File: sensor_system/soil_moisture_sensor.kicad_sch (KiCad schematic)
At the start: 15 parts, among them U1 TLC555xD, U2 XC6206PxxxMR

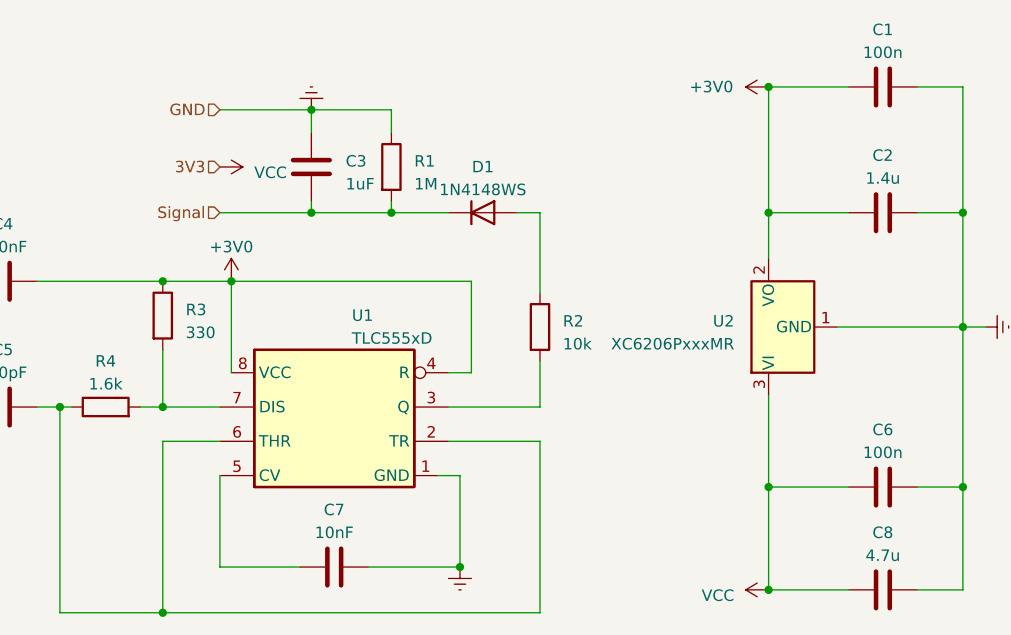
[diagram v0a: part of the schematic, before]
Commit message: Pievienoti footprint visām komponentēm
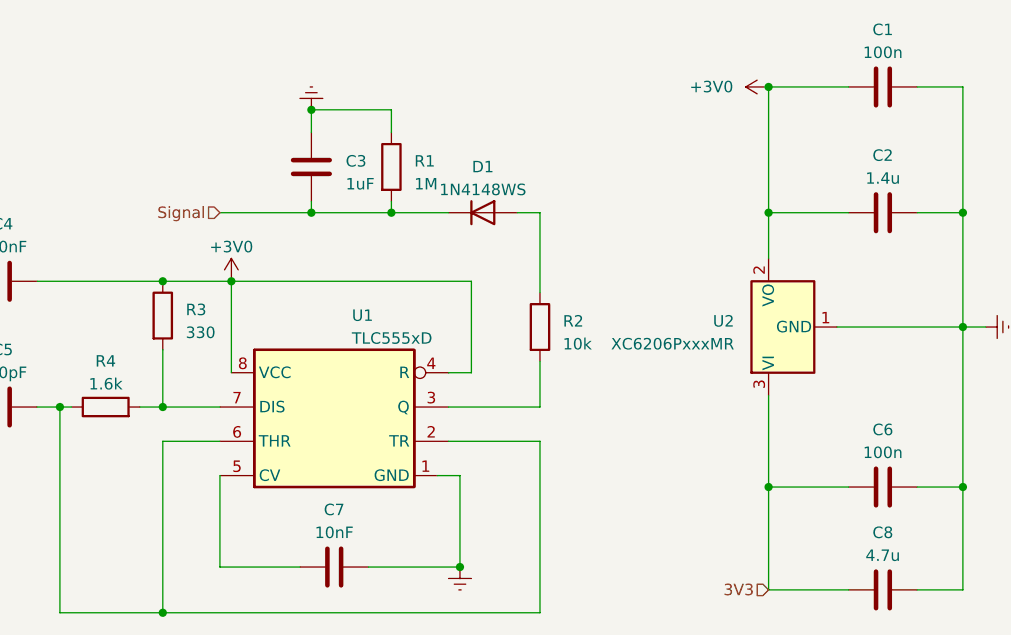
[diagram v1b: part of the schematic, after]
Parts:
- C1, C4, C5, C6, C7, R1, R2, R3, R4: footprint (none) -> Resistor_SMD:R_0805_2012Metric
- C2, C8: footprint (none) -> Capacitor_SMD:C_0805_2012Metric
- C3: footprint (none) -> Capacitor_SMD:C_0603_1608Metric
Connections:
- net VCC renamed 3V3
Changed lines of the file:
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@@
   (junction (at 149.86 95.25) (diameter 0) (color 0 0 0 0)
   )
-  (junction (at 200.66 137.16) (diameter 0) (color 0 0 0 0)
-  )
   (junction (at 158.75 95.25) (diameter 0) (color 0 0 0 0)
   )
@@
     (stroke (width 0) (type default))
   )
+  (wire (pts (xy 200.66 137.16) (xy 209.55 137.16))
+    (stroke (width 0) (type default))
+  )
   (wire (pts (xy 200.66 95.25) (xy 209.55 95.25))
     (stroke (width 0) (type default))
@@
     (stroke (width 0) (type default))
   )
-  (wire (pts (xy 200.66 137.16) (xy 200.66 125.73))
-    (stroke (width 0) (type default))
-  )
   (wire (pts (xy 222.25 125.73) (xy 222.25 107.95))
     (stroke (width 0) (type default))
@@
     (stroke (width 0) (type default))
   )
-  (wire (pts (xy 209.55 137.16) (xy 200.66 137.16))
-    (stroke (width 0) (type default))
-  )
   (wire (pts (xy 121.92 116.84) (xy 123.19 116.84))
     (stroke (width 0) (type default))
@@
     (stroke (width 0) (type default))
   )
-  (wire (pts (xy 139.7 83.82) (xy 149.86 83.82))
-    (stroke (width 0) (type default))
-  )
   (wire (pts (xy 222.25 125.73) (xy 222.25 137.16))
     (stroke (width 0) (type default))
@@
     (stroke (width 0) (type default))
   )
+  (wire (pts (xy 200.66 125.73) (xy 200.66 137.16))
+    (stroke (width 0) (type default))
+  )
   (wire (pts (xy 217.17 125.73) (xy 222.25 125.73))
     (stroke (width 0) (type default))
@@
     (stroke (width 0) (type default))
   )
-  (hierarchical_label "3V3" (shape input) (at 139.7 90.17 180) (fields_autoplaced)
+  (hierarchical_label "3V3" (shape input) (at 200.66 137.16 180) (fields_autoplaced)
     (effects (font (size 1.27 1.27)) (justify right))
   )
   (hierarchical_label "Signal" (shape input) (at 139.7 95.25 180) (fields_autoplaced)
-    (effects (font (size 1.27 1.27)) (justify right))
-  )
-  (hierarchical_label "GND" (shape input) (at 139.7 83.82 180) (fields_autoplaced)
     (effects (font (size 1.27 1.27)) (justify right))
   )
@@
       (effects (font (size 1.27 1.27)))
     )
-    (property "Footprint" "" (at 217.17 124.7648 0)
+    (property "Footprint" "Resistor_SMD:R_0805_2012Metric" (at 217.17 124.7648 0)
       (effects (font (size 1.27 1.27)) hide)
     )
@@
       (effects (font (size 1.27 1.27)))
     )
-    (property "Footprint" "" (at 119.38 101.9048 0)
+    (property "Footprint" "Resistor_SMD:R_0805_2012Metric" (at 119.38 101.9048 0)
       (effects (font (size 1.27 1.27)) hide)
     )
@@
       (effects (font (size 1.27 1.27)))
     )
-    (property "Footprint" "" (at 119.38 115.8748 0)
+    (property "Footprint" "Resistor_SMD:R_0805_2012Metric" (at 119.38 115.8748 0)
       (effects (font (size 1.27 1.27)) hide)
     )
@@
       (effects (font (size 1.27 1.27)))
     )
-    (property "Footprint" "" (at 127 118.618 90)
+    (property "Footprint" "Resistor_SMD:R_0805_2012Metric" (at 127 118.618 90)
       (effects (font (size 1.27 1.27)) hide)
     )
@@
       (effects (font (size 1.27 1.27)))
     )
-    (property "Footprint" "" (at 156.21 133.6548 0)
+    (property "Footprint" "Resistor_SMD:R_0805_2012Metric" (at 156.21 133.6548 0)
       (effects (font (size 1.27 1.27)) hide)
     )
@@
       (effects (font (size 1.27 1.27)))
     )
-    (property "Footprint" "" (at 217.17 94.2848 0)
+    (property "Footprint" "Capacitor_SMD:C_0805_2012Metric" (at 217.17 94.2848 0)
       (effects (font (size 1.27 1.27)) hide)
     )
@@
       (effects (font (size 1.27 1.27)) (justify left))
     )
-    (property "Footprint" "" (at 150.8252 93.98 0)
+    (property "Footprint" "Capacitor_SMD:C_0603_1608Metric" (at 150.8252 93.98 0)
       (effects (font (size 1.27 1.27)) hide)
     )
@@
       (effects (font (size 1.27 1.27)) (justify left))
     )
-    (property "Footprint" "" (at 131.572 106.68 90)
+    (property "Footprint" "Resistor_SMD:R_0805_2012Metric" (at 131.572 106.68 90)
       (effects (font (size 1.27 1.27)) hide)
     )
@@
       (effects (font (size 1.27 1.27)) (justify left))
     )
-    (property "Footprint" "" (at 156.972 90.17 90)
+    (property "Footprint" "Resistor_SMD:R_0805_2012Metric" (at 156.972 90.17 90)
       (effects (font (size 1.27 1.27)) hide)
     )
@@
       (effects (font (size 1.27 1.27)) (justify left))
     )
-    (property "Footprint" "" (at 173.482 107.95 90)
+    (property "Footprint" "Resistor_SMD:R_0805_2012Metric" (at 173.482 107.95 90)
       (effects (font (size 1.27 1.27)) hide)
     )
@@
       (effects (font (size 1.27 1.27)))
     )
-    (property "Footprint" "" (at 217.17 136.1948 0)
+    (property "Footprint" "Capacitor_SMD:C_0805_2012Metric" (at 217.17 136.1948 0)
       (effects (font (size 1.27 1.27)) hide)
     )
@@
       (effects (font (size 1.27 1.27)))
     )
-    (property "Footprint" "" (at 217.17 80.3148 0)
+    (property "Footprint" "Resistor_SMD:R_0805_2012Metric" (at 217.17 80.3148 0)
       (effects (font (size 1.27 1.27)) hide)
     )
@@
         )
       )
-    )
-  )
-  (symbol (lib_id "power:VCC") (at 200.66 137.16 90) (unit 1)
-    (in_bom yes) (on_board yes) (dnp no) (fields_autoplaced)
-    (property "Reference" "#PWR08" (at 204.47 137.16 0)
-      (effects (font (size 1.27 1.27)) hide)
-    )
-    (property "Value" "VCC" (at 196.85 137.795 90)
-      (effects (font (size 1.27 1.27)) (justify left))
-    )
-    (property "Footprint" "" (at 200.66 137.16 0)
-      (effects (font (size 1.27 1.27)) hide)
-    )
-    (property "Datasheet" "" (at 200.66 137.16 0)
-      (effects (font (size 1.27 1.27)) hide)
-    )
-    (pin "1")
-    (instances
-      (project "sensor_system"
-        (path "/d745cb62-8f4d-408c-9af8-25e31ee1e0d0/aa2079c6-27cc-4f87-ae93-44912efb1889"
-          (reference "#PWR08") (unit 1)
-        )
-      )
-    )
-  )
-  (symbol (lib_id "power:VCC") (at 139.7 90.17 270) (unit 1)
-    (in_bom yes) (on_board yes) (dnp no) (fields_autoplaced)
-    (property "Reference" "#PWR04" (at 135.89 90.17 0)
-      (effects (font (size 1.27 1.27)) hide)
-    )
-    (property "Value" "VCC" (at 143.51 90.805 90)
-      (effects (font (size 1.27 1.27)) (justify left))
-    )
-    (property "Footprint" "" (at 139.7 90.17 0)
-      (effects (font (size 1.27 1.27)) hide)
-    )
-    (property "Datasheet" "" (at 139.7 90.17 0)
-      (effects (font (size 1.27 1.27)) hide)
-    )
-    (pin "1")
-    (instances
-      (project "sensor_system"
-        (path "/d745cb62-8f4d-408c-9af8-25e31ee1e0d0/aa2079c6-27cc-4f87-ae93-44912efb1889"
-          (reference "#PWR04") (unit 1)
-        )
-      )

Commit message: Disaster in progress
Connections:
- net +3V0 renamed 3V
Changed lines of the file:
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@@
 (kicad_sch (version 20230121) (generator eeschema)
   (paper "A4")
-  (junction (at 200.66 81.28) (diameter 0) (color 0 0 0 0)
-  )
   (junction (at 140.97 102.87) (diameter 0) (color 0 0 0 0)
   )
@@
     (stroke (width 0) (type default))
   )
-  (wire (pts (xy 167.64 102.87) (xy 140.97 102.87))
-    (stroke (width 0) (type default))
-  )
   (wire (pts (xy 149.86 95.25) (xy 158.75 95.25))
     (stroke (width 0) (type default))
@@
     (stroke (width 0) (type default))
   )
+  (wire (pts (xy 140.97 102.87) (xy 167.64 102.87))
+    (stroke (width 0) (type default))
+  )
   (wire (pts (xy 200.66 137.16) (xy 209.55 137.16))
     (stroke (width 0) (type default))
@@
     (stroke (width 0) (type default))
   )
+  (wire (pts (xy 158.75 83.82) (xy 158.75 86.36))
+    (stroke (width 0) (type default))
+  )
+  (wire (pts (xy 140.97 102.87) (xy 133.35 102.87))
+    (stroke (width 0) (type default))
+  )
+  (wire (pts (xy 140.97 102.87) (xy 140.97 113.03))
+    (stroke (width 0) (type default))
+  )
+  (wire (pts (xy 175.26 95.25) (xy 172.72 95.25))
+    (stroke (width 0) (type default))
+  )
+  (wire (pts (xy 156.21 134.62) (xy 166.37 134.62))
+    (stroke (width 0) (type default))
+  )
+  (wire (pts (xy 222.25 125.73) (xy 222.25 137.16))
+    (stroke (width 0) (type default))
+  )
+  (wire (pts (xy 133.35 120.65) (xy 133.35 139.7))
+    (stroke (width 0) (type default))
+  )
+  (wire (pts (xy 208.28 107.95) (xy 222.25 107.95))
+    (stroke (width 0) (type default))
+  )
+  (wire (pts (xy 167.64 113.03) (xy 167.64 102.87))
+    (stroke (width 0) (type default))
+  )
+  (wire (pts (xy 200.66 100.33) (xy 200.66 95.25))
+    (stroke (width 0) (type default))
+  )
+  (wire (pts (xy 166.37 124.46) (xy 163.83 124.46))
+    (stroke (width 0) (type default))
+  )
+  (wire (pts (xy 200.66 125.73) (xy 200.66 137.16))
+    (stroke (width 0) (type default))
+  )
+  (wire (pts (xy 217.17 125.73) (xy 222.25 125.73))
+    (stroke (width 0) (type default))
+  )
   (wire (pts (xy 200.66 81.28) (xy 209.55 81.28))
     (stroke (width 0) (type default))
   )
-  (wire (pts (xy 158.75 83.82) (xy 158.75 86.36))
-    (stroke (width 0) (type default))
-  )
-  (wire (pts (xy 140.97 102.87) (xy 133.35 102.87))
-    (stroke (width 0) (type default))
-  )
-  (wire (pts (xy 140.97 102.87) (xy 140.97 113.03))
-    (stroke (width 0) (type default))
-  )
-  (wire (pts (xy 175.26 95.25) (xy 172.72 95.25))
-    (stroke (width 0) (type default))
-  )
-  (wire (pts (xy 156.21 134.62) (xy 166.37 134.62))
-    (stroke (width 0) (type default))
-  )
-  (wire (pts (xy 222.25 125.73) (xy 222.25 137.16))
-    (stroke (width 0) (type default))
-  )
-  (wire (pts (xy 133.35 120.65) (xy 133.35 139.7))
-    (stroke (width 0) (type default))
-  )
-  (wire (pts (xy 208.28 107.95) (xy 222.25 107.95))
-    (stroke (width 0) (type default))
-  )
-  (wire (pts (xy 167.64 113.03) (xy 167.64 102.87))
-    (stroke (width 0) (type default))
-  )
-  (wire (pts (xy 200.66 100.33) (xy 200.66 95.25))
-    (stroke (width 0) (type default))
-  )
-  (wire (pts (xy 166.37 124.46) (xy 163.83 124.46))
-    (stroke (width 0) (type default))
-  )
-  (wire (pts (xy 200.66 125.73) (xy 200.66 137.16))
-    (stroke (width 0) (type default))
-  )
-  (wire (pts (xy 217.17 125.73) (xy 222.25 125.73))
-    (stroke (width 0) (type default))
-  )
   (wire (pts (xy 217.17 81.28) (xy 222.25 81.28))
     (stroke (width 0) (type default))
@@
   (wire (pts (xy 133.35 116.84) (xy 139.7 116.84))
     (stroke (width 0) (type default))
+  )
+  (global_label "3V" (shape input) (at 200.66 81.28 180) (fields_autoplaced)
+    (effects (font (size 1.27 1.27)) (justify right))
+    (property "Intersheetrefs" "${INTERSHEET_REFS}" (at 189.1061 81.28 0)
+      (effects (font (size 1.27 1.27)) (justify right) hide)
+    )
+  )
+  (global_label "3V" (shape input) (at 140.97 102.87 90) (fields_autoplaced)
+    (effects (font (size 1.27 1.27)) (justify left))
+    (property "Intersheetrefs" "${INTERSHEET_REFS}" (at 140.97 97.6661 90)
+      (effects (font (size 1.27 1.27)) (justify left) hide)
+    )
   )
   (hierarchical_label "3V3" (shape input) (at 200.66 137.16 180) (fields_autoplaced)
@@
     )
   )
-  (symbol (lib_id "power:+3V0") (at 200.66 81.28 90) (unit 1)
-    (in_bom yes) (on_board yes) (dnp no)
-    (property "Reference" "#PWR07" (at 204.47 81.28 0)
-      (effects (font (size 1.27 1.27)) hide)
-    )
-    (property "Value" "+3V0" (at 194.31 81.28 90)
-      (effects (font (size 1.27 1.27)))
-    )
-    (property "Footprint" "" (at 200.66 81.28 0)
-      (effects (font (size 1.27 1.27)) hide)
-    )
-    (property "Datasheet" "" (at 200.66 81.28 0)
-      (effects (font (size 1.27 1.27)) hide)
-    )
-    (pin "1")
-    (instances
-      (project "sensor_system"
-        (path "/d745cb62-8f4d-408c-9af8-25e31ee1e0d0/aa2079c6-27cc-4f87-ae93-44912efb1889"
-          (reference "#PWR07") (unit 1)
-        )
-      )
-    )
-  )
   (symbol (lib_id "Device:C") (at 213.36 95.25 90) (unit 1)
     (in_bom yes) (on_board yes) (dnp no) (fields_autoplaced)
@@
         )
       )
-    )
-  )
-  (symbol (lib_id "power:+3V0") (at 140.97 102.87 0) (unit 1)
-    (in_bom yes) (on_board yes) (dnp no) (fields_autoplaced)
-    (property "Reference" "#PWR05" (at 140.97 106.68 0)
-      (effects (font (size 1.27 1.27)) hide)
-    )
-    (property "Value" "+3V0" (at 140.97 99.06 0)
-      (effects (font (size 1.27 1.27)))
-    )
-    (property "Footprint" "" (at 140.97 102.87 0)
-      (effects (font (size 1.27 1.27)) hide)
-    )
-    (property "Datasheet" "" (at 140.97 102.87 0)
-      (effects (font (size 1.27 1.27)) hide)
-    )
-    (pin "1")
-    (instances
-      (project "sensor_system"
-        (path "/d745cb62-8f4d-408c-9af8-25e31ee1e0d0/aa2079c6-27cc-4f87-ae93-44912efb1889"
-          (reference "#PWR05") (unit 1)
-        )
-      )

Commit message: Board fix 2.0
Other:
- moved on the sheet: C1, C2, C6, C8, U2

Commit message: Gala versija
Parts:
- added TP1: TestPoint, Connector_PinHeader_1.00mm:PinHeader_1x01_P1.00mm_Vertical, symbol Connector:TestPoint
- added TP2, TP4: IN Soil, symbol Connector:TestPoint
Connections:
- net 3V: now also TP1.1
- net Earth: now also TP4.1
- net at U1.3 (Q): now also R2.1; no longer R2.2
- net at D1.2 (A): now also R2.2, TP2.1; no longer R2.1
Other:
- moved on the sheet: C1, C2, C3, C4, C5, C6, C7, C8, D1, R1, R2, R3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
